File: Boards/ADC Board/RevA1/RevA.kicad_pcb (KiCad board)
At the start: 2 copper layers, 85 x 56 mm, 31 parts, among them J1 Left Connector, J10 Jumper Terminals, J11 Arduino Nano, J12 Arduino Nano, J13 Extra Pins, J14 Screw Terminals, J16 Screw Terminals, J2 Right Connector, J3 Screw Terminals, J4 Jumper Terminals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

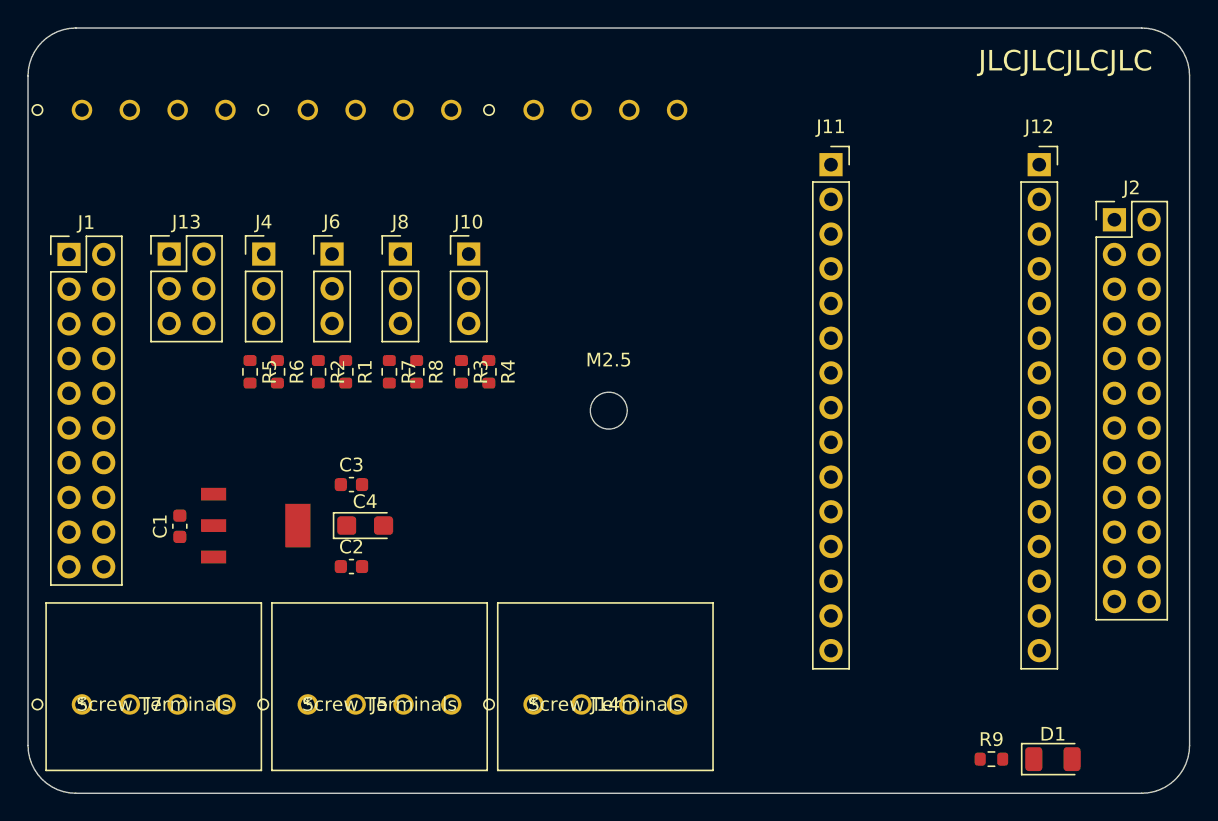
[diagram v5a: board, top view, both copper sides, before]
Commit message: Finished placing and organizing PCB components for the ADC board, and prepped board for auto-routing.
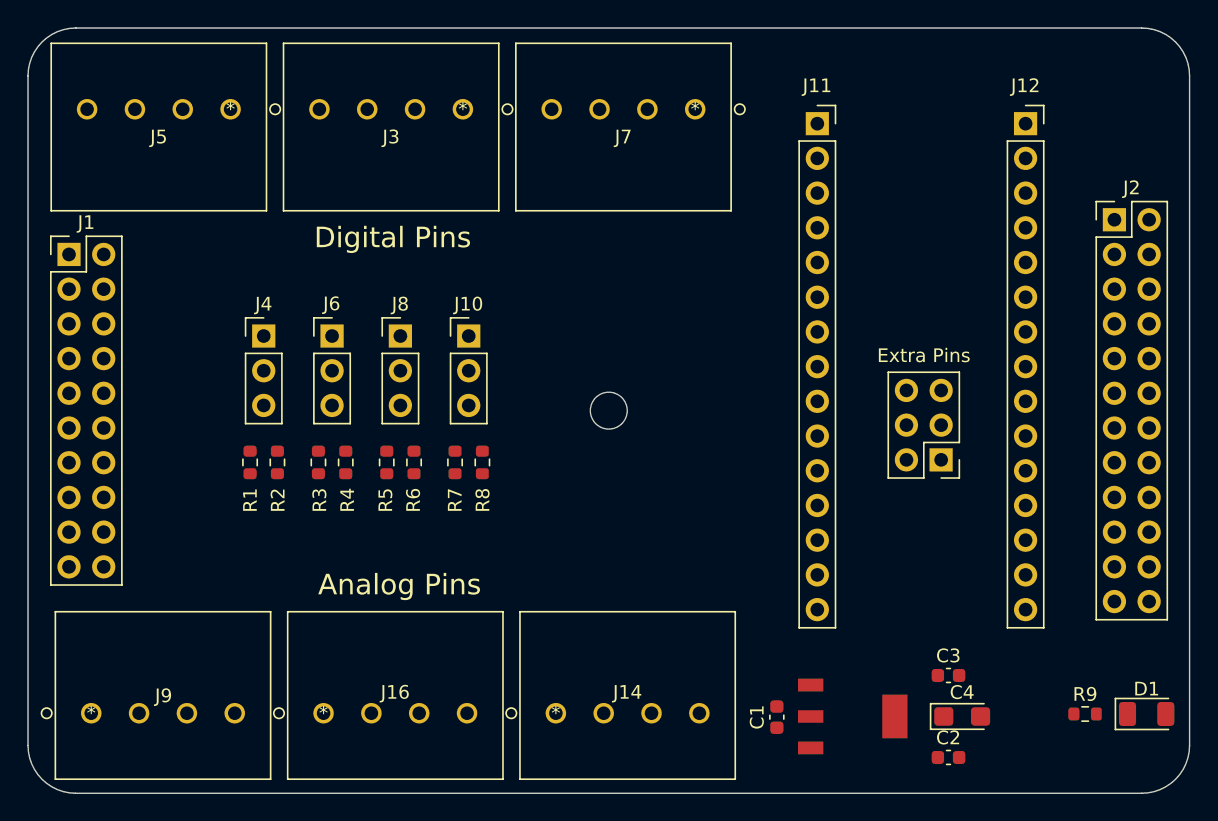
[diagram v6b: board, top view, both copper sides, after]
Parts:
- J16, J3, J9: moved to F.Cu
- moved J7 62.5 mm to (208.8, 75.9), turned to 180 degrees
- moved J13 58.5 mm to (226.8, 101.6), turned to 180 degrees
- moved J9 54.7 mm to (164.6, 120.1)
- moved J16 47.6 mm to (181.6, 120.1)
- moved C2 45.9 mm to (227.4, 123.4)
- moved C3 45.9 mm to (227.4, 117.4)
- moved C4 45.9 mm to (228.4, 120.4)
- moved VR1 45.9 mm to (220.4, 120.4)
- moved C1 45.9 mm to (214.8, 120.4)
- moved J5 43.9 mm to (174.8, 75.9), turned to 180 degrees
- moved R3 12.4 mm to (181.2, 101.8)
- moved R4 12.4 mm to (183.2, 101.8)
- moved R5 12.0 mm to (186.2, 101.8)
- moved R6 12.0 mm to (188.2, 101.8)
- moved J3 11.3 mm to (191.8, 75.9), turned to 180 degrees
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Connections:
- J14 pad 2: /Analog_0 -> /5V
- J14 pad 3: /5V -> /Analog_3
- J14 pad 4: (no net) -> /GND
- J16 pad 1: /GND -> /Analog_1
- J16 pad 2: /Analog_2 -> /GND
- J16 pad 4: (no net) -> /Analog_2
- J3 pad 1: /GND -> /Digital_2
- J3 pad 2: /Digital_0 -> /5V
- J3 pad 3: /5V -> /GND
- J3 pad 4: (no net) -> /Digital_1
- J5 pad 1: /GND -> /5V
- J5 pad 2: /Digital_1 -> /GND
- J5 pad 3: /5V -> /Digital_0
- J5 pad 4: (no net) -> /5V
- J7 pad 2: /Digital_2 -> /Digital_3
- J7 pad 4: (no net) -> /GND
- J9 pad 1: /GND -> /5V
- J9 pad 2: /Digital_3 -> /Analog_0
- J9 pad 3: /5V -> /GND
- J9 pad 4: (no net) -> /5V
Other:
- board text added: "Analog Pins"
- board text added: "Digital Pins"
